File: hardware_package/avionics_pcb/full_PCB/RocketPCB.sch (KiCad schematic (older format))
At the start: 77 parts, among them J1 USB_C_Receptacle, J2 Micro_SD_Card, J3 Conn_01x03_Female, M1 Motor_Servo_JR, M2 Motor_Servo_JR, Q1 DMG2301L, Q2 Q_PMOS_DGS, SW1 SW_Push, SW2 SW_Push, U1 STM32F405RGTx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

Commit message: Removed additional oscillators.
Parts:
- removed C1, C2, C3, C7: 22pF, Capacitor_THT:CP_Radial_D5.0mm_P2.50mm, symbol Device:C
- removed Y1: 12MHz, Oscillator:Oscillator_DIP-14_LargePads, symbol Device:Crystal
- removed Y2: 32MHz, Oscillator:Oscillator_DIP-8_LargePads, symbol Device:Crystal
- U3: symbol radio_header:Radio_Header -> RocketPCB-rescue:Radio_Header-radio_header
- U5: symbol flash_memory:W25Q16JV -> RocketPCB-rescue:W25Q16JV-flash_memory
- U8: symbol gps_header:GPS_header -> RocketPCB-rescue:GPS_header-gps_header
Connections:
- wire segments 408 -> 395
- no-connect marks 40 -> 43
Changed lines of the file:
@@
 DACs
-$Comp
-L Device:C C1
-U 1 1 5F34E284
-P 4300 4000
-F 0 "C1" H 4415 4046 50  0000 L CNN
-F 1 "22pF" H 4415 3955 50  0000 L CNN
-F 2 "Capacitor_THT:CP_Radial_D5.0mm_P2.50mm" H 4338 3850 50  0001 C CNN
-F 3 "~" H 4300 4000 50  0001 C CNN
-	1    4300 4000
-	1    0    0    -1
-$EndComp
-$Comp
-L power:GND #PWR010
-U 1 1 5F34FAF1
-P 4300 4150
-F 0 "#PWR010" H 4300 3900 50  0001 C CNN
-F 1 "GND" H 4305 3977 50  0000 C CNN
-F 2 "" H 4300 4150 50  0001 C CNN
-F 3 "" H 4300 4150 50  0001 C CNN
-	1    4300 4150
-	1    0    0    -1
-$EndComp
-Wire Wire Line
-	4300 3850 4300 3650
-Wire Wire Line
-	4300 3650 4450 3650
-Wire Wire Line
-	4300 3650 4300 3200
-Connection ~ 4300 3650
 $Comp
 L Connector:USB_C_Receptacle J1
@@
 $EndComp
 Wire Wire Line
-	4950 3300 6150 3300
-Wire Wire Line
-	4950 3650 4950 3300
-Wire Wire Line
 	7650 3000 7550 3000
 Wire Wire Line
@@
 Wire Wire Line
 	6150 3500 5800 3500
-Wire Wire Line
-	4300 3200 6150 3200
 Wire Wire Line
 	6750 5400 6750 5500
@@
 Text Label 6150 3500 2    50   ~ 0
 SDIO_CMD
-Connection ~ 4950 3650
-Wire Wire Line
-	4950 3650 4950 3850
-Wire Wire Line
-	4750 3650 4950 3650
-$Comp
-L power:GND #PWR011
-U 1 1 5F350220
-P 4950 4150
-F 0 "#PWR011" H 4950 3900 50  0001 C CNN
-F 1 "GND" H 4955 3977 50  0000 C CNN
-F 2 "" H 4950 4150 50  0001 C CNN
-F 3 "" H 4950 4150 50  0001 C CNN
-	1    4950 4150
-	1    0    0    -1
-$EndComp
-$Comp
-L Device:C C2
-U 1 1 5F34F563
-P 4950 4000
-F 0 "C2" H 5065 4046 50  0000 L CNN
-F 1 "22pF" H 5065 3955 50  0000 L CNN
-F 2 "Capacitor_THT:CP_Radial_D5.0mm_P2.50mm" H 4988 3850 50  0001 C CNN
-F 3 "~" H 4950 4000 50  0001 C CNN
-	1    4950 4000
-	1    0    0    -1
-$EndComp
-$Comp
-L Device:Crystal Y1
-U 1 1 5F34C8EB
-P 4600 3650
-F 0 "Y1" H 4600 3918 50  0000 C CNN
-F 1 "12MHz" H 4600 3827 50  0000 C CNN
-F 2 "Oscillator:Oscillator_DIP-14_LargePads" H 4600 3650 50  0001 C CNN
-F 3 "~" H 4600 3650 50  0001 C CNN
-	1    4600 3650
-	1    0    0    -1
-$EndComp
 Text Label 6150 4900 2    50   ~ 0
 SDIO_CLK
@@
 Wire Wire Line
 	6650 1250 6650 1800
-Wire Wire Line
-	5150 5700 5150 5450
-$Comp
-L Device:C C3
-U 1 1 5F33BF27
-P 5150 5850
-F 0 "C3" H 5265 5896 50  0000 L CNN
-F 1 "22pF" H 5265 5805 50  0000 L CNN
-F 2 "Capacitor_THT:CP_Radial_D5.0mm_P2.50mm" H 5188 5700 50  0001 C CNN
-F 3 "~" H 5150 5850 50  0001 C CNN
-	1    5150 5850
-	1    0    0    -1
-$EndComp
-$Comp
-L Device:C C7
-U 1 1 5F33D1AE
-P 5650 5850
-F 0 "C7" H 5765 5896 50  0000 L CNN
-F 1 "22pF" H 5765 5805 50  0000 L CNN
-F 2 "Capacitor_THT:CP_Radial_D5.0mm_P2.50mm" H 5688 5700 50  0001 C CNN
-F 3 "~" H 5650 5850 50  0001 C CNN
-	1    5650 5850
-	1    0    0    -1
-$EndComp
-$Comp
-L Device:Crystal Y2
-U 1 1 5F33DA69
-P 5400 5450
-F 0 "Y2" H 5400 5718 50  0000 C CNN
-F 1 "32MHz" H 5400 5627 50  0000 C CNN
-F 2 "Oscillator:Oscillator_DIP-8_LargePads" H 5400 5450 50  0001 C CNN
-F 3 "~" H 5400 5450 50  0001 C CNN
-	1    5400 5450
-	1    0    0    -1
-$EndComp
-Wire Wire Line
-	5250 5450 5150 5450
-Wire Wire Line
-	5550 5450 5650 5450
-Wire Wire Line
-	5650 5450 5650 5700
-$Comp
-L power:GND #PWR016
-U 1 1 5F34B2CF
-P 5650 6000
-F 0 "#PWR016" H 5650 5750 50  0001 C CNN
-F 1 "GND" H 5655 5827 50  0000 C CNN
-F 2 "" H 5650 6000 50  0001 C CNN
-F 3 "" H 5650 6000 50  0001 C CNN
-	1    5650 6000
-	1    0    0    -1
-$EndComp
-$Comp
-L power:GND #PWR013
-U 1 1 5F34BAA6
-P 5150 6000
-F 0 "#PWR013" H 5150 5750 50  0001 C CNN
-F 1 "GND" H 5155 5827 50  0000 C CNN
-F 2 "" H 5150 6000 50  0001 C CNN
-F 3 "" H 5150 6000 50  0001 C CNN
-	1    5150 6000
-	1    0    0    -1
-$EndComp
 Connection ~ 9350 10450
 Wire Wire Line
@@
 Wire Wire Line
 	8350 9450 8450 9450
-Wire Wire Line
-	5150 5100 5150 5450
-Wire Wire Line
-	5150 5100 5650 5100
-Connection ~ 5150 5450
-Wire Wire Line
-	5650 5100 5650 5450
-Connection ~ 5650 5100
-Wire Wire Line
-	5650 5100 6150 5100
-Connection ~ 5650 5450
-$Comp
-L gps_header:GPS_header U8
+$Comp
+L RocketPCB-rescue:GPS_header-gps_header U8
 U 1 1 5F7E44DB
 P 13800 8950
@@
 $EndComp
 $Comp
-L radio_header:Radio_Header U3
+L RocketPCB-rescue:Radio_Header-radio_header U3
 U 1 1 5F7F38B6
 P 11150 4350
@@
 16M-BIT SERIAL FLASH MEMORY
 $Comp
-L flash_memory:W25Q16JV U5
+L RocketPCB-rescue:W25Q16JV-flash_memory U5
 U 1 1 5F7BE5CF
 P 11100 6850
@@
 Wire Wire Line
 	1000 8200 1150 8200
+Wire Wire Line
+	6150 3200 5800 3200
+Wire Wire Line
+	6150 3300 5800 3300
+Wire Wire Line
+	6150 5100 5800 5100
+NoConn ~ 5800 5100
+NoConn ~ 5800 3300
+NoConn ~ 5800 3200
 $EndSCHEMATC

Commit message: Combined two of the regulators, reassigned footprints, added pull up R
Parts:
- removed C22: 10uF, Capacitor_THT:CP_Radial_D5.0mm_P2.50mm, symbol Device:C
- removed C25: 1uF, Capacitor_THT:CP_Radial_D5.0mm_P2.50mm, symbol Device:C
- removed D3: MBR0540, Diode_SMD:D_SOD-123, symbol Diode:MBR0540
- removed L1: 2.2uH, Inductor_THT:L_Axial_L9.5mm_D4.0mm_P12.70mm_Horizontal_Fastron_SMCC, symbol Device:L
- removed Q2: Q_PMOS_DGS, symbol Device:Q_PMOS_DGS
- removed R19: 10k, Resistor_THT:R_Axial_DIN0207_L6.3mm_D2.5mm_P7.62mm_Horizontal, symbol Device:R
- removed U2: TPS62160DSG, Package_SON:WSON-8-1EP_2x2mm_P0.5mm_EP0.9x1.6mm_ThermalVias, symbol Regulator_Switching:TPS62160DSG
- removed U6: AP2112K-3.3, Package_TO_SOT_SMD:SOT-23-5, symbol Regulator_Linear:AP2112K-3.3
- added C1, C3: 1uF, Capacitor_SMD:C_0603_1608Metric, symbol Device:C
- added C2: 10uF, Capacitor_SMD:C_0805_2012Metric, symbol Device:C
- added C7: C, Capacitor_SMD:C_0603_1608Metric, symbol Device:C
- added D2: MBR0540, Diode_SMD:D_SOD-123, symbol Diode:MBR0540
- added Q?: DMG2301L, Package_TO_SOT_SMD:SOT-23, symbol Transistor_FET:DMG2301L
- added R17: 4.7k, Resistor_SMD:R_0603_1608Metric, symbol Device:R
- added U2: UCC381DP-3, 3v3 _linReg:SOIC127P599X175-8N, symbol UCC381DP-3:UCC381DP-3
- C10, C16: value 10uF -> 0.1uF; footprint Capacitor_THT:CP_Radial_D5.0mm_P2.50mm -> Capacitor_SMD:C_0603_1608Metric
- C11: value 22uF -> 0.1uF; footprint Capacitor_THT:CP_Radial_D5.0mm_P2.50mm -> Capacitor_SMD:C_0603_1608Metric
- C12, C15, C20, C28, C31, C32, C33, C4, C6, C9: footprint Capacitor_THT:CP_Radial_D5.0mm_P2.50mm -> Capacitor_SMD:C_0805_2012Metric
- C13: value 0.1u -> 0.1uF; footprint Capacitor_THT:CP_Radial_D5.0mm_P2.50mm -> Capacitor_SMD:C_0603_1608Metric
- C14: value 2.2u -> 2.2uF; footprint Capacitor_THT:CP_Radial_D5.0mm_P2.50mm -> Capacitor_SMD:C_0603_1608Metric
- C17, C18, C19, C21, C23, C24, C26, C27, C29, C30, C5, C8: footprint Capacitor_THT:CP_Radial_D5.0mm_P2.50mm -> Capacitor_SMD:C_0603_1608Metric
- D1: footprint LED_THT:LED_D5.0mm_Clear -> LED_SMD:LED_0603_1608Metric_Pad1.05x0.95mm_HandSolder
- M1, M2: footprint (none) -> GPS_head0:JR_connector_3pin
- R1, R15, R16, R2, R3, R4, R5, R6, R7: footprint Resistor_THT:R_Axial_DIN0207_L6.3mm_D2.5mm_P7.62mm_Horizontal -> Resistor_SMD:R_0603_1608Metric
- R10: value 100k -> 10k; footprint Resistor_THT:R_Axial_DIN0207_L6.3mm_D2.5mm_P7.62mm_Horizontal -> Resistor_SMD:R_0603_1608Metric
- R11: value 649k -> 100k; footprint Resistor_THT:R_Axial_DIN0207_L6.3mm_D2.5mm_P7.62mm_Horizontal -> Resistor_SMD:R_0603_1608Metric
- R12: value 180k -> 4.7K; footprint Resistor_THT:R_Axial_DIN0207_L6.3mm_D2.5mm_P7.62mm_Horizontal -> Resistor_SMD:R_0603_1608Metric
- R13: value 100k -> 4.7k; footprint Resistor_THT:R_Axial_DIN0207_L6.3mm_D2.5mm_P7.62mm_Horizontal -> Resistor_SMD:R_0603_1608Metric
- R14, R8, R9: footprint Resistor_THT:R_Axial_DIN0204_L3.6mm_D1.6mm_P7.62mm_Horizontal -> Resistor_SMD:R_0603_1608Metric
- TP1: footprint (none) -> TestPoint:TestPoint_Pad_D1.0mm
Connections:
- net labels removed: +3.3V, +3V7, PG
- wire segments 395 -> 384
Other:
- note added: "3.3V out"
- note removed: "3.3V Regulator for peripherals\n"
- note removed: "3.7V out"
- note removed: "Filter\n"
- moved on the sheet: J2, R1

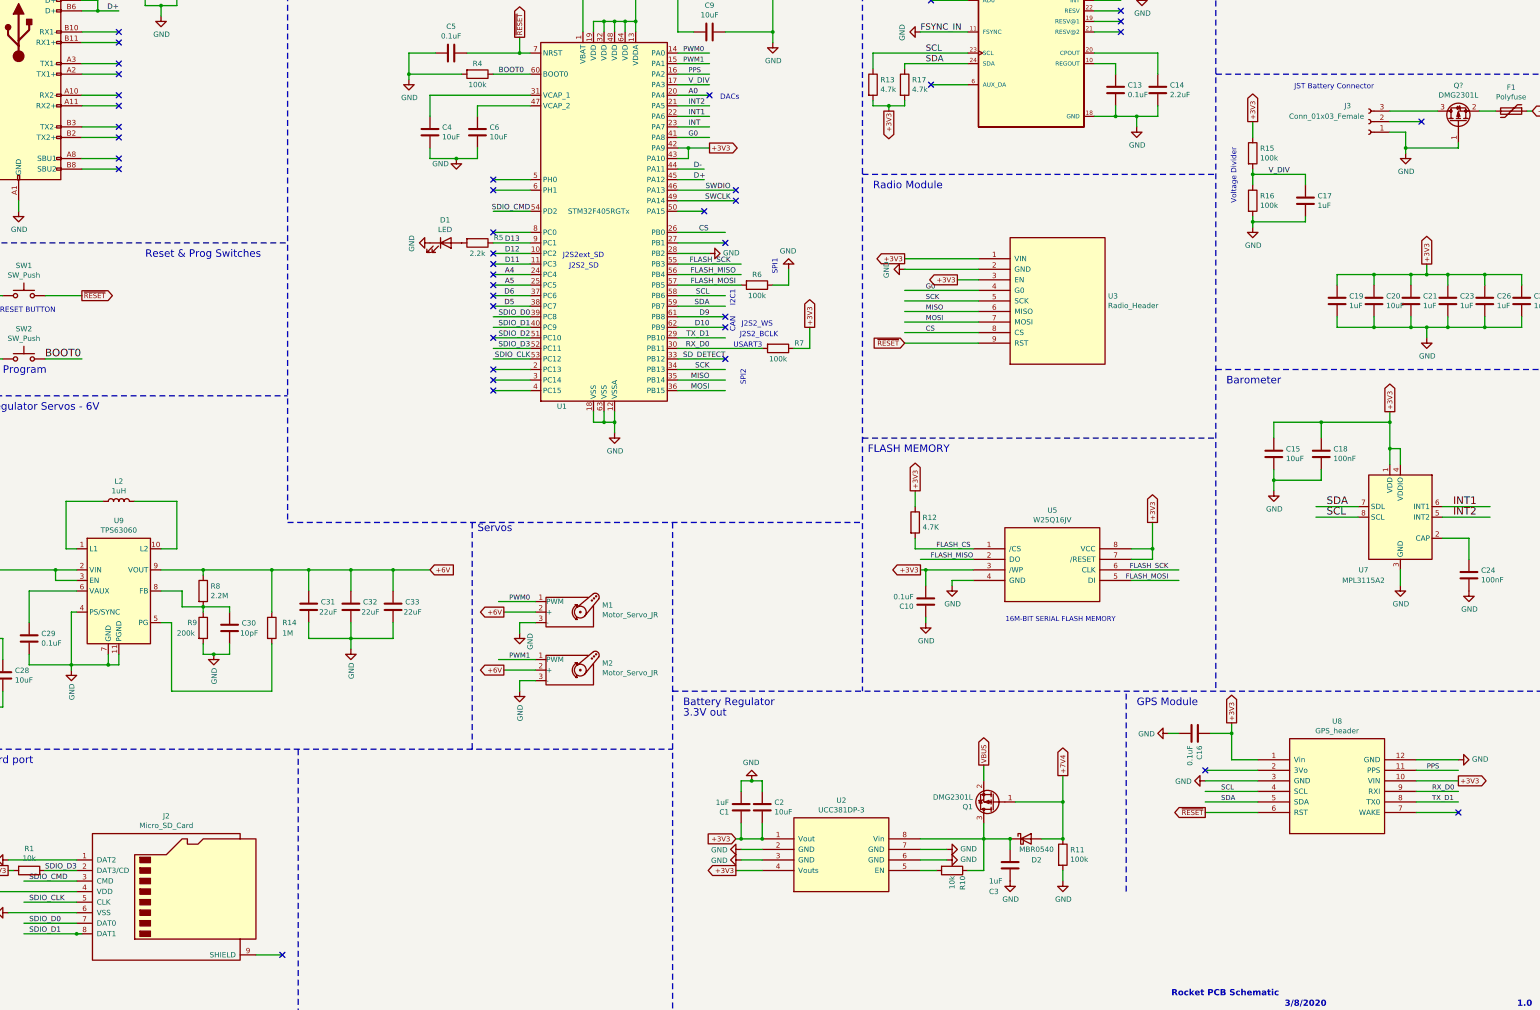
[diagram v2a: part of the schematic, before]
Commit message: Added test points and LEDs for debug, also added decoupling capacitors
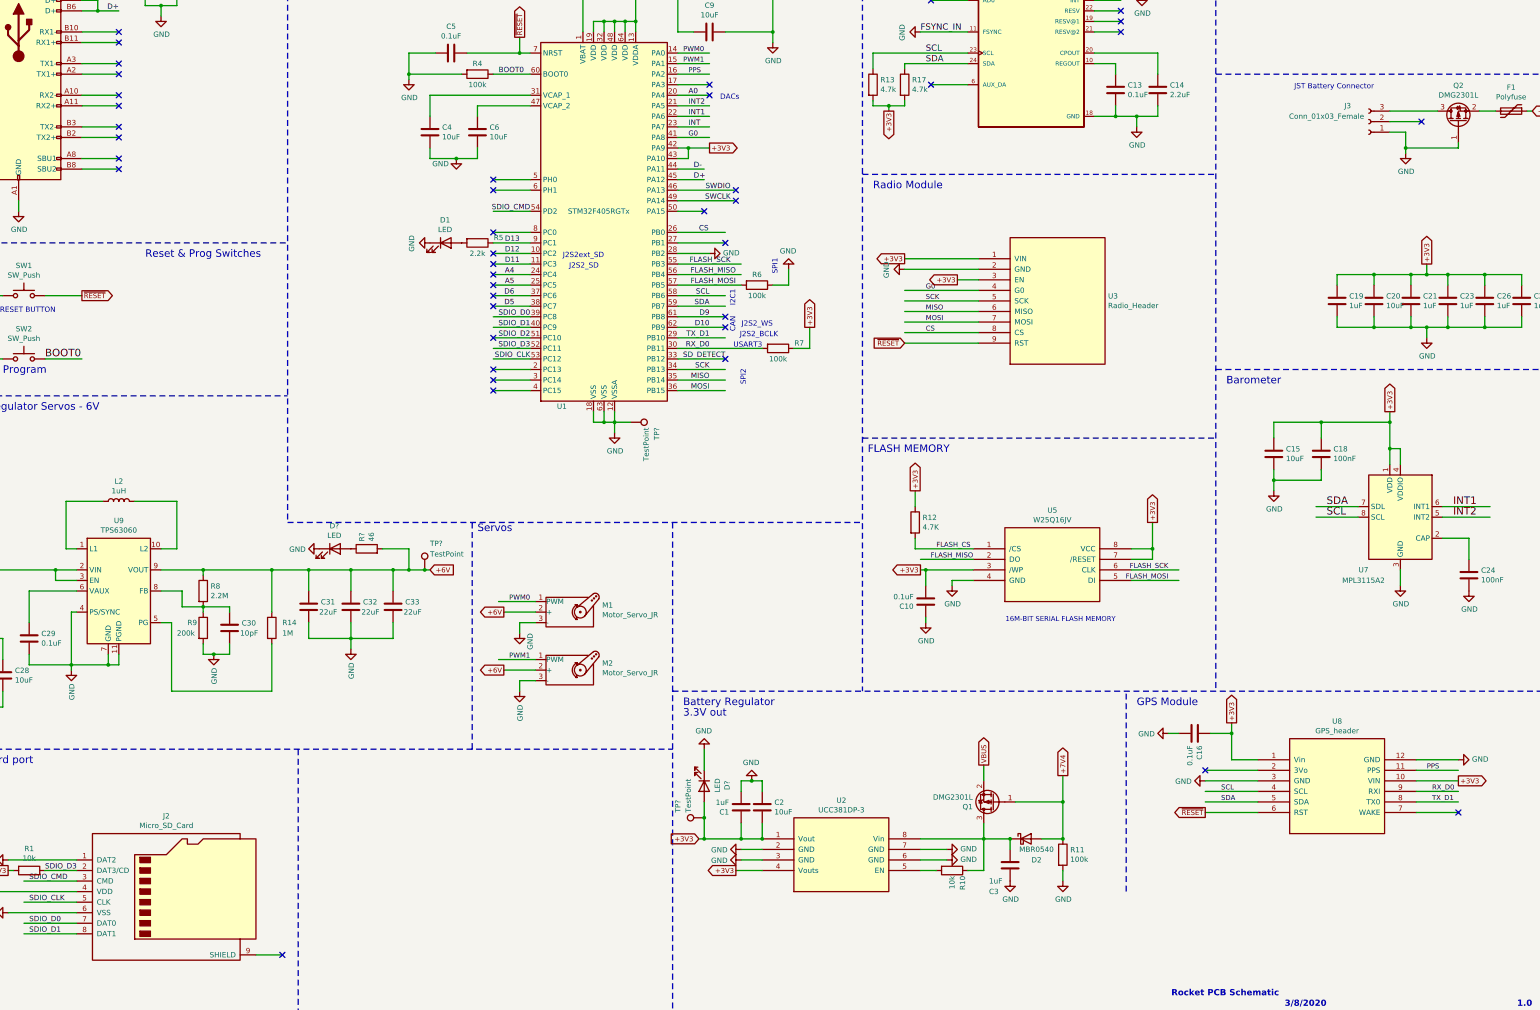
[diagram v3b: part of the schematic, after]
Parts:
- removed C17: 1uF, Capacitor_SMD:C_0603_1608Metric, symbol Device:C
- removed R15, R16: 100k, Resistor_SMD:R_0603_1608Metric, symbol Device:R
- added D? (x2): LED, LED_SMD:LED_0603_1608Metric_Pad1.05x0.95mm_HandSolder, symbol Device:LED
- added R?: 46, Resistor_SMD:R_0603_1608Metric, symbol Device:R
- added TP? (x3): TestPoint, TestPoint:TestPoint_Pad_D1.0mm, symbol Connector:TestPoint
- SW1, SW2: footprint Button_Switch_THT:SW_PUSH-12mm -> Button_Switch_SMD:SW_Push_SPST_NO_Alps_SKRK
- gave numbers to parts that had none: 1
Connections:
- net labels removed: V_DIV
- wire segments 384 -> 383
- no-connect marks 43 -> 44
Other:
- note removed: "Voltage Divider"
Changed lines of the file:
@@
 Wire Wire Line
 	5500 2200 5000 2200
-Text Label 7650 2300 0    50   ~ 0
-V_DIV
 Text Label 5850 2200 0    50   ~ 0
 BOOT0
@@
 F 0 "SW1" H 1350 4585 50  0000 C CNN
 F 1 "SW_Push" H 1350 4494 50  0000 C CNN
-F 2 "Button_Switch_THT:SW_PUSH-12mm" H 1350 4500 50  0001 C CNN
+F 2 "Button_Switch_SMD:SW_Push_SPST_NO_Alps_SKRK" H 1350 4500 50  0001 C CNN
 F 3 "~" H 1350 4500 50  0001 C CNN
 	1    1350 4300
@@
 RESET BUTTON\n\n
 $Comp
-L Device:R R15
-U 1 1 5F4E7BC3
-P 13000 2950
-F 0 "R15" H 13070 2996 50  0000 L CNN
-F 1 "100k" H 13070 2905 50  0000 L CNN
-F 2 "Resistor_SMD:R_0603_1608Metric" V 12930 2950 50  0001 C CNN
-F 3 "~" H 13000 2950 50  0001 C CNN
-	1    13000 2950
-	1    0    0    -1
-$EndComp
-$Comp
-L Device:R R16
-U 1 1 5F4E8272
-P 13000 3400
-F 0 "R16" H 13070 3446 50  0000 L CNN
-F 1 "100k" H 13070 3355 50  0000 L CNN
-F 2 "Resistor_SMD:R_0603_1608Metric" V 12930 3400 50  0001 C CNN
-F 3 "~" H 13000 3400 50  0001 C CNN
-	1    13000 3400
-	1    0    0    -1
-$EndComp
-Wire Wire Line
-	13000 2650 13000 2800
-Wire Wire Line
-	13000 3100 13000 3150
-$Comp
-L power:GND #PWR045
-U 1 1 5F4F8513
-P 13000 3650
-F 0 "#PWR045" H 13000 3400 50  0001 C CNN
-F 1 "GND" H 13005 3477 50  0000 C CNN
-F 2 "" H 13000 3650 50  0001 C CNN
-F 3 "" H 13000 3650 50  0001 C CNN
-	1    13000 3650
-	1    0    0    -1
-$EndComp
-Wire Wire Line
-	13000 3550 13000 3600
-$Comp
-L Device:C C17
-U 1 1 5F508EDD
-P 13500 3400
-F 0 "C17" H 13615 3446 50  0000 L CNN
-F 1 "1uF" H 13615 3355 50  0000 L CNN
-F 2 "Capacitor_SMD:C_0603_1608Metric" H 13538 3250 50  0001 C CNN
-F 3 "~" H 13500 3400 50  0001 C CNN
-	1    13500 3400
-	1    0    0    -1
-$EndComp
-Wire Wire Line
-	13000 3150 13500 3150
-Wire Wire Line
-	13500 3150 13500 3250
-Connection ~ 13000 3150
-Wire Wire Line
-	13000 3150 13000 3250
-$Comp
 L Connector:Conn_01x03_Female J3
 U 1 1 5F51AC89
@@
 Text Notes 14150 2350 2    50   ~ 0
 JST Battery Connector\n
-Text Notes 12850 2900 3    50   ~ 0
-Voltage Divider
 Text Notes 2750 650  0    71   ~ 0
 USB-C Connector\n
@@
 Wire Notes Line
 	12650 500  12650 8050
-Text Label 13150 3150 0    50   ~ 0
-V_DIV
 Text Notes 8100 4400 1    50   ~ 0
 I2C1
@@
 Text Label 1400 10250 0    50   ~ 0
 SDIO_D0
-Wire Wire Line
-	1900 10350 1850 10350
-Connection ~ 1850 10350
-Wire Wire Line
-	1850 10350 1350 10350
 Text Label 1400 10350 0    50   ~ 0
 SDIO_D1
@@
 F 0 "SW2" H 1350 5185 50  0000 C CNN
 F 1 "SW_Push" H 1350 5094 50  0000 C CNN
-F 2 "Button_Switch_THT:SW_PUSH-12mm" H 1350 5100 50  0001 C CNN
+F 2 "Button_Switch_SMD:SW_Push_SPST_NO_Alps_SKRK" H 1350 5100 50  0001 C CNN
 F 3 "~" H 1350 5100 50  0001 C CNN
 	1    1350 4900
@@
 	4850 7550 4450 7550
 Wire Wire Line
-	4850 6900 5200 6900
+	4850 6900 5000 6900
 Wire Wire Line
 	4450 6900 4850 6900
@@
 VBUS
 Wire Wire Line
-	13500 3550 13500 3600
-Wire Wire Line
-	13500 3600 13000 3600
-Connection ~ 13000 3600
-Wire Wire Line
-	13000 3600 13000 3650
-Wire Wire Line
 	900  8200 1000 8200
 $Comp
@@
 	0    1    1    0
 $EndComp
-Text GLabel 8100 9450 0    47   Input ~ 0
+Text GLabel 7750 9450 0    47   Input ~ 0
 +3V3
-Wire Wire Line
-	8100 9450 8150 9450
 Text GLabel 8100 9750 0    47   Output ~ 0
 +3V3
@@
 	11200 9100 11200 8850
 Connection ~ 11200 9100
-Text GLabel 13000 2650 1    47   Output ~ 0
-+3V3
 $Comp
 L Device:R R12
@@
 	9400 2000 10300 2000
 $Comp
-L Transistor_FET:DMG2301L Q?
+L Transistor_FET:DMG2301L Q2
 U 1 1 6048B4F6
 P 14950 2650
-F 0 "Q?" V 15292 2650 50  0000 C CNN
+F 0 "Q2" V 15292 2650 50  0000 C CNN
 F 1 "DMG2301L" V 15201 2650 50  0000 C CNN
 F 2 "Package_TO_SOT_SMD:SOT-23" H 15150 2575 50  0001 L CIN
@@
 	0    -1   -1   0
 $EndComp
+NoConn ~ 7850 2300
+$Comp
+L Device:LED D?
+U 1 1 5F856AA9
+P 7800 8950
+F 0 "D?" H 7793 9167 50  0000 C CNN
+F 1 "LED" H 7793 9076 50  0000 C CNN
+F 2 "LED_SMD:LED_0603_1608Metric_Pad1.05x0.95mm_HandSolder" H 7800 8950 50  0001 C CNN
+F 3 "~" H 7800 8950 50  0001 C CNN
+	1    7800 8950
+	0    1    1    0
+$EndComp
+Wire Wire Line
+	1850 10350 1350 10350
+Wire Wire Line
+	7750 9450 7800 9450
+Wire Wire Line
+	7800 9450 7800 9250
+Connection ~ 7800 9450
+Wire Wire Line
+	7800 9450 8150 9450
+Wire Wire Line
+	7800 8800 7800 8600
+$Comp
+L power:GND #PWR?
+U 1 1 5F96333D
+P 7800 8600
+F 0 "#PWR?" H 7800 8350 50  0001 C CNN
+F 1 "GND" H 7805 8427 50  0000 C CNN
+F 2 "" H 7800 8600 50  0001 C CNN
+F 3 "" H 7800 8600 50  0001 C CNN
+	1    7800 8600
+	-1   0    0    1
+$EndComp
+$Comp
+L Connector:TestPoint TP?
+U 1 1 5F966683
+P 7800 9250
+F 0 "TP?" H 7850 9500 50  0000 L CNN
+F 1 "TestPoint" H 7850 9400 50  0000 L CNN
+F 2 "TestPoint:TestPoint_Pad_D1.0mm" H 8000 9250 50  0001 C CNN
+F 3 "~" H 8000 9250 50  0001 C CNN
+	1    7800 9250
+	0    -1   -1   0
+$EndComp
+Connection ~ 7800 9250
+Wire Wire Line
+	7800 9250 7800 9100
+$Comp
+L Connector:TestPoint TP?
+U 1 1 5F983E00
+P 5150 6900
+F 0 "TP?" H 5200 7150 50  0000 L CNN
+F 1 "TestPoint" H 5200 7050 50  0000 L CNN
+F 2 "TestPoint:TestPoint_Pad_D1.0mm" H 5350 6900 50  0001 C CNN
+F 3 "~" H 5350 6900 50  0001 C CNN
+	1    5150 6900
+	1    0    0    -1
+$EndComp
+Connection ~ 5150 6900
+Wire Wire Line
+	5150 6900 5200 6900
+$Comp
+L Device:LED D?
+U 1 1 5F987713
+P 4300 6700
+F 0 "D?" H 4293 6917 50  0000 C CNN
+F 1 "LED" H 4293 6826 50  0000 C CNN
+F 2 "LED_SMD:LED_0603_1608Metric_Pad1.05x0.95mm_HandSolder" H 4300 6700 50  0001 C CNN
+F 3 "~" H 4300 6700 50  0001 C CNN
+	1    4300 6700
+	1    0    0    -1
+$EndComp
+$Comp
+L power:GND #PWR?
+U 1 1 5F989A8C
+P 4150 6700
+F 0 "#PWR?" H 4150 6450 50  0001 C CNN
+F 1 "GND" V 4155 6572 50  0000 R CNN
+F 2 "" H 4150 6700 50  0001 C CNN
+F 3 "" H 4150 6700 50  0001 C CNN
+	1    4150 6700
+	0    1    1    0
+$EndComp
+Wire Wire Line
+	5000 6700 5000 6900
+Connection ~ 5000 6900
+Wire Wire Line
+	5000 6900 5150 6900
+$Comp
+L Device:R R?
+U 1 1 5F9EC1AC
+P 4600 6700
+F 0 "R?" H 4670 6746 50  0000 L CNN
+F 1 "46" H 4670 6655 50  0000 L CNN
+F 2 "Resistor_SMD:R_0603_1608Metric" V 4530 6700 50  0001 C CNN
+F 3 "~" H 4600 6700 50  0001 C CNN
+	1    4600 6700
+	0    -1   -1   0
+$EndComp
+Wire Wire Line
+	4750 6700 5000 6700
+$Comp
+L Connector:TestPoint TP?
+U 1 1 5FA5605A
+P 7100 5500
+F 0 "TP?" H 7150 5750 50  0000 L CNN
+F 1 "TestPoint" H 7150 5650 50  0000 L CNN
+F 2 "TestPoint:TestPoint_Pad_D1.0mm" H 7300 5500 50  0001 C CNN
+F 3 "~" H 7300 5500 50  0001 C CNN
+	1    7100 5500
+	0    1    1    0
+$EndComp
+Wire Wire Line
+	6950 5500 7100 5500
 $EndSCHEMATC
